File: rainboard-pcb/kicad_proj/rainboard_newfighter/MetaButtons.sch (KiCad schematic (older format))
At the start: 7 parts

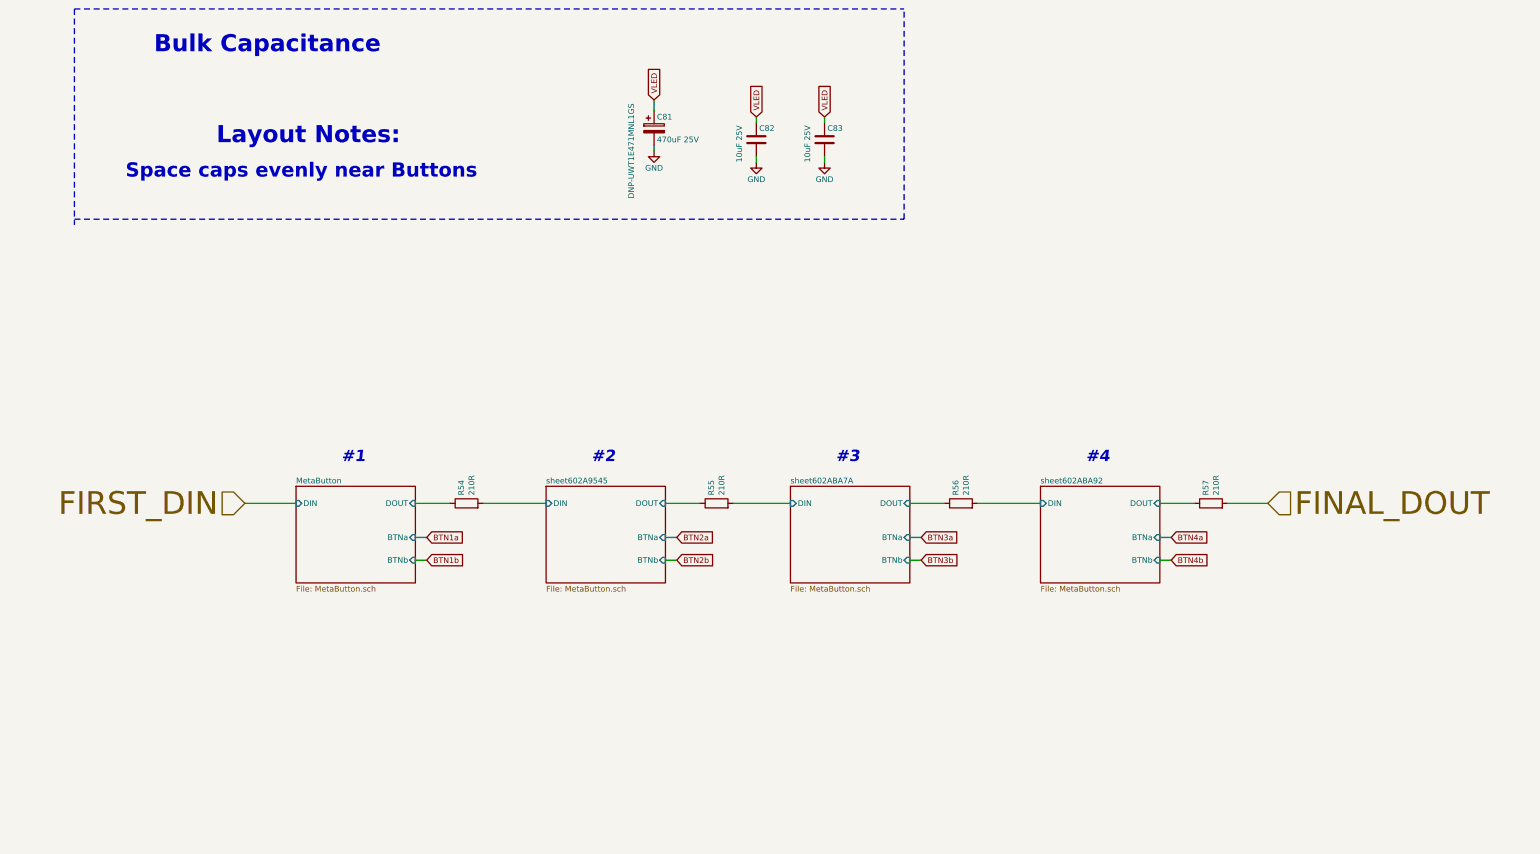
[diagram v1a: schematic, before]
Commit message: Removed RGB from buttons, part numbers updated, cleaned up schematic
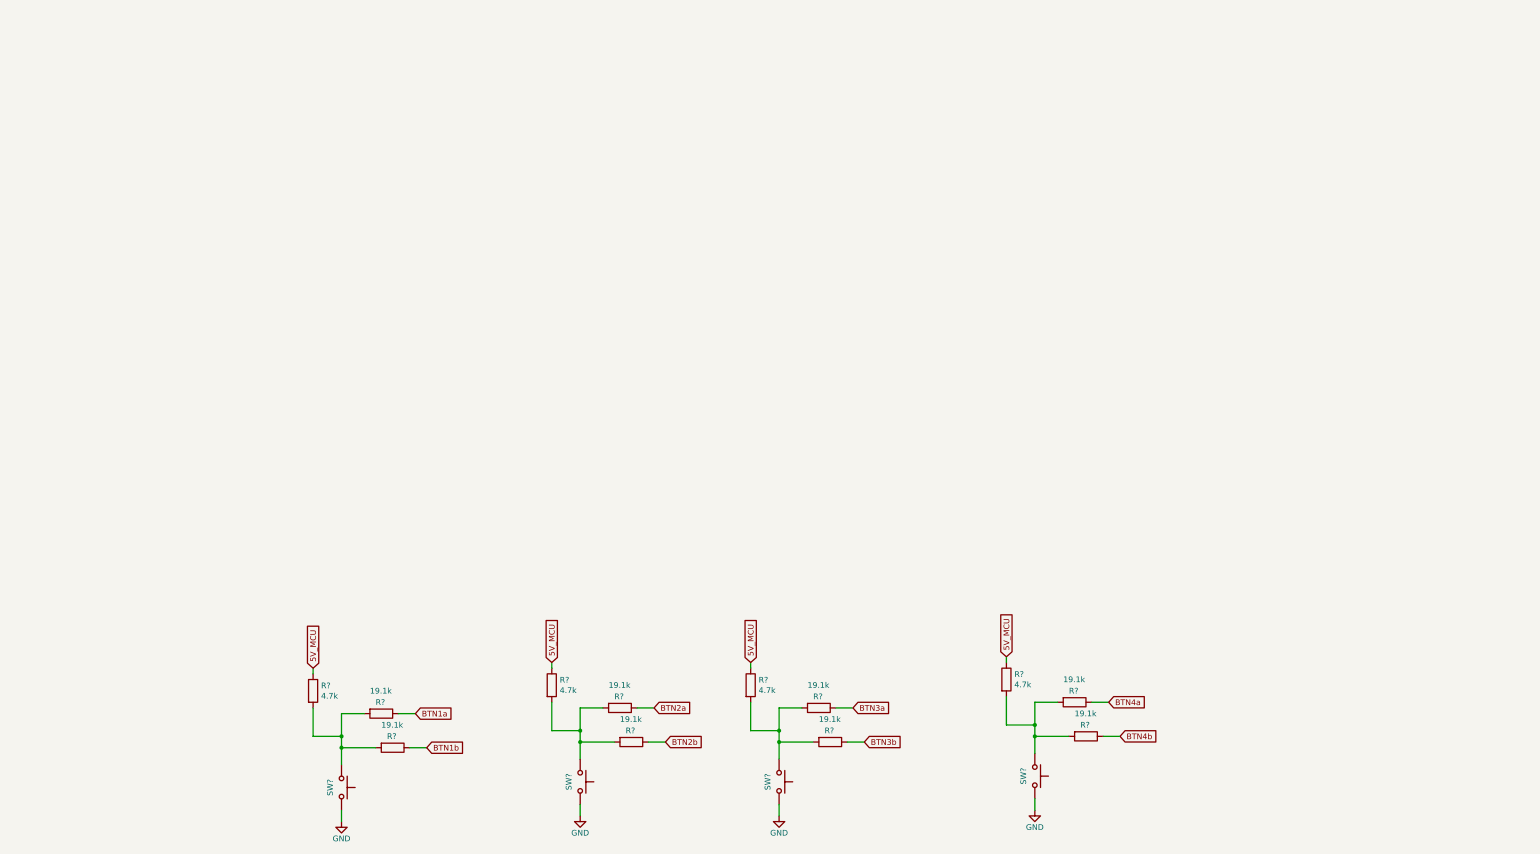
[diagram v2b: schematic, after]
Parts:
- removed C81: 470uF 25V, Capacitor_SMD:CP_Elec_10x10, symbol lib_symbol:CP
- removed C82, C83: 10uF 25V, Capacitor_SMD:C_1206_3216Metric, symbol lib_symbol:C
- removed R54, R55, R56, R57: 210R, Resistor_SMD:R_0805_2012Metric, symbol Device:R
- added R? (x4): 4.7k, Resistor_SMD:R_0603_1608Metric, symbol Device:R
- added R? (x8): 19.1k, Resistor_SMD:R_0603_1608Metric, symbol Device:R
- added SW? (x4): SANWA-OBSF24, symbol lib_symbol:SANWA-OBSF24
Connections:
- net BTN1a: now also R?.1
- net BTN1b: now also R?.1
- net BTN2a: now also R?.1
- net BTN2b: now also R?.1
- net BTN3a: now also R?.1
- net BTN3b: now also R?.1
- net BTN4a: now also R?.1
- net BTN4b: now also R?.1
- net GND: now also SW?.2, SW?.2, SW?.2, SW?.2
- new net: R?.2, R?.2, R?.2, SW?.1 (x4)
- new net 5V_MCU: R?.1, R?.1, R?.1, R?.1
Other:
- note removed: "#1"
- note removed: "#2"
- note removed: "#3"
- note removed: "#4"
- note removed: "Bulk Capacitance"
- note removed: "Layout Notes:"
- note removed: "Space caps evenly near Buttons"
